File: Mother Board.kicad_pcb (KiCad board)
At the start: 4 copper layers, 93 x 151 mm, 103 parts, among them J1 Conn_01x04, J2 USB_B_Mini, J3 Conn_02x05_Odd_Even, J4 Conn_01x04, J5 Conn_01x03, J6 Conn_01x03, J7 Conn_01x04, SW1 SW_Push, U1 SC189, U2 TPS2121, U3 FT232RL, U4 TPS2121, U5 STM32F407VGTx, U6 W25Q128JV-DTR, U7 SN74LVC1G04DBVR, Y1 Crystal_GND24

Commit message: Needs final clean up, then ready for ordering
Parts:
- added 3v3_MUX_ST1: TestPoint, TestPoint:TestPoint_Pad_D1.0mm, F.Cu at (101.5, 143.5)
- added 5V_MUX_ST1: TestPoint, TestPoint:TestPoint_Pad_D1.0mm, F.Cu at (96.5, 143.5)
- added D10: LED, LED_SMD:LED_1206_3216Metric_Pad1.42x1.75mm_HandSolder, F.Cu at (104.5, 64.0)
- added D11: LED, LED_SMD:LED_1206_3216Metric_Pad1.42x1.75mm_HandSolder, F.Cu at (98.0, 64.0)
- added D5: LED, LED_SMD:LED_1206_3216Metric_Pad1.42x1.75mm_HandSolder, F.Cu at (172.0, 177.0)
- added D6: LED, LED_SMD:LED_1206_3216Metric_Pad1.42x1.75mm_HandSolder, F.Cu at (160.5, 64.0)
- added D7: LED, LED_SMD:LED_1206_3216Metric_Pad1.42x1.75mm_HandSolder, F.Cu at (154.0, 64.0)
- added D8: LED, LED_SMD:LED_1206_3216Metric_Pad1.42x1.75mm_HandSolder, F.Cu at (132.5, 64.0)
- added D9: LED, LED_SMD:LED_1206_3216Metric_Pad1.42x1.75mm_HandSolder, F.Cu at (126.0, 64.0)
- added Q1: Q_NMOS_GSD, Package_TO_SOT_SMD:SOT-323_SC-70_Handsoldering, F.Cu at (172.0, 185.0)
- added Q2: Q_NMOS_GSD, Package_TO_SOT_SMD:SOT-323_SC-70_Handsoldering, F.Cu at (160.5, 72.0)
- added Q3: Q_NMOS_GSD, Package_TO_SOT_SMD:SOT-323_SC-70_Handsoldering, F.Cu at (154.0, 72.0)
- added Q4: Q_NMOS_GSD, Package_TO_SOT_SMD:SOT-323_SC-70_Handsoldering, F.Cu at (132.5, 72.0)
- added Q5: Q_NMOS_GSD, Package_TO_SOT_SMD:SOT-323_SC-70_Handsoldering, F.Cu at (126.0, 72.0)
- added Q6: Q_NMOS_GSD, Package_TO_SOT_SMD:SOT-323_SC-70_Handsoldering, F.Cu at (104.5, 72.0)
- added Q7: Q_NMOS_GSD, Package_TO_SOT_SMD:SOT-323_SC-70_Handsoldering, F.Cu at (98.0, 72.0)
- added R10: 10k, Resistor_SMD:R_0603_1608Metric_Pad1.05x0.95mm_HandSolder, F.Cu at (172.0, 190.0)
- added R11: 330R, Resistor_SMD:R_0603_1608Metric_Pad1.05x0.95mm_HandSolder, F.Cu at (172.0, 180.5)
- added R44: 10k, Resistor_SMD:R_0603_1608Metric_Pad1.05x0.95mm_HandSolder, F.Cu at (160.5, 77.0)
- added R45: 10k, Resistor_SMD:R_0603_1608Metric_Pad1.05x0.95mm_HandSolder, F.Cu at (154.0, 77.0)
- added R46: 330R, Resistor_SMD:R_0603_1608Metric_Pad1.05x0.95mm_HandSolder, F.Cu at (160.5, 67.0)
- added R47: 330R, Resistor_SMD:R_0603_1608Metric_Pad1.05x0.95mm_HandSolder, F.Cu at (154.0, 67.0)
- added R48: 10k, Resistor_SMD:R_0603_1608Metric_Pad1.05x0.95mm_HandSolder, F.Cu at (132.5, 77.0)
- added R49: 10k, Resistor_SMD:R_0603_1608Metric_Pad1.05x0.95mm_HandSolder, F.Cu at (126.0, 77.0)
- added R50: 330R, Resistor_SMD:R_0603_1608Metric_Pad1.05x0.95mm_HandSolder, F.Cu at (132.5, 67.5)
- added R51: 330R, Resistor_SMD:R_0603_1608Metric_Pad1.05x0.95mm_HandSolder, F.Cu at (126.0, 67.5)
- added R52: 10k, Resistor_SMD:R_0603_1608Metric_Pad1.05x0.95mm_HandSolder, F.Cu at (104.6, 77.0)
- added R53: 10k, Resistor_SMD:R_0603_1608Metric_Pad1.05x0.95mm_HandSolder, F.Cu at (98.0, 77.0)
- added R54: 330R, Resistor_SMD:R_0603_1608Metric_Pad1.05x0.95mm_HandSolder, F.Cu at (104.6, 67.5)
- added R55: 330R, Resistor_SMD:R_0603_1608Metric_Pad1.05x0.95mm_HandSolder, F.Cu at (98.0, 67.5)
- added SPI_FLASH_CS1: TestPoint, test_points_mdg:TestPoint_Keystone_5015_Micro-Minature, F.Cu at (123.5, 121.0)
- added USART3_CTS1: TestPoint, test_points_mdg:TestPoint_Keystone_5015_Micro-Minature, F.Cu at (129.5, 201.0)
- added USART3_RTS1: TestPoint, test_points_mdg:TestPoint_Keystone_5015_Micro-Minature, F.Cu at (134.5, 201.0)
- added USART3_RX1: TestPoint, test_points_mdg:TestPoint_Keystone_5015_Micro-Minature, F.Cu at (124.5, 201.0)
- added USART3_TX1: TestPoint, test_points_mdg:TestPoint_Keystone_5015_Micro-Minature, F.Cu at (119.5, 201.0)
- GND1, GND2, GND3, GND4, GND5, I2C1_SCL1, I2C1_SDA1, SPI3_MISO1, SPI3_MOSI1, SPI3_SCK1: footprint test_points_mdg:Keystone_5010 -> test_points_mdg:TestPoint_Keystone_5015_Micro-Minature
- moved GND1 5.00 mm to (87.5, 63.0)
- moved REF** 5.00 mm to (143.0, 67.0)
- moved REF** 5.00 mm to (171.0, 67.0)
- moved REF** 5.00 mm to (115.0, 67.0)
- moved GND3 1.00 mm to (172.0, 76.0)
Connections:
- U5 pad 33: Net-(U5-Pad33) -> MICRO_STATUS
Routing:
- net CARD0_ENABLE: track 114.7 -> 187.0 mm, vias 1 -> 2
- net +3V3: track 110.8 -> 179.2 mm, vias 33 -> 40
- net CARD0_STATUS: track 128.4 -> 169.8 mm, vias 1 -> 2
- net MICRO_STATUS: track 0.00 -> 41.2 mm, vias 0 -> 2
- net GND: track 116.4 -> 157.5 mm, vias 69 -> 86
- net CARD4_ENABLE: track 229.4 -> 260.5 mm
- net CARD4_STATUS: track 239.1 -> 264.1 mm
- net CARD1_ENABLE: track 203.1 -> 224.5 mm, vias 1 -> 2
- net Net-(3v3_MUX_ST1-Pad1): track 4.05 -> 20.8 mm
- net CARD1_STATUS: track 211.2 -> 226.0 mm, vias 1 -> 2
- net Net-(5V_MUX_ST1-Pad1): track 17.2 -> 29.2 mm
- net USART3_CTS: track 63.7 -> 69.9 mm
- net USART3_RX: track 51.6 -> 57.1 mm
- net Net-(Q3-Pad3): track 0.00 -> 4.03 mm
- net Net-(Q2-Pad3): track 0.00 -> 4.03 mm
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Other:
- board size 93 x 151 mm -> 93 x 146 mm
- board text added: "24V 24V 5V 5V"
- board text added: "24V 24V 5V 5V 3.3V 3.3V GND GND I2C1_SDA I2C1_SCL ADD0 ADD1 ADD2 ENABLE STATUS GPIO5 GPIO4 GPIO3 GPIO2 SENSE+ GND GND"
- board text added: "24V 24V 5V 5V 3.3V 3.3V GND GND SPI3_SCK SPI3_MISO SPI3_MOSI CS TIM1CH1 TIM1CH1N TIM3CH1 TIM2CH1 TIM9CH1 GPIO0 GPIO1 SENSE- GND GND"
- board text added: "24V 24V 5V 5V 3.3V 3.3V GND GND SPI3_SCK SPI3_MISO SPI3_MOSI CS TIM8_CH1 TIM8_CH1N TIM5_CH1 TIM4_CH1 TIM12_CH2 GPIO0 GPIO1 SENSE - GND GND"
- board text added: "3V3 3V3 GND GND"
- board text added: "3V3 STAT"
- board text added: "5V STAT"
- board text added: "CARD0"
- board text added: "CARD0 ENABLE"
- board text added: "CARD0 STATUS"
- board text added: "CARD1"
- board text added: "CARD1 ENABLE"
- board text added: "CARD1 STATUS"
- board text added: "CARD4"
- board text added: "CARD4 ENABLE"
- board text added: "CARD4 STATUS"
- board text added: "GND GND GND GND"
- board text added: "MICRO STATUS"
- board text added: "RESET"
- board text added: "RX"
- board text added: "TX"

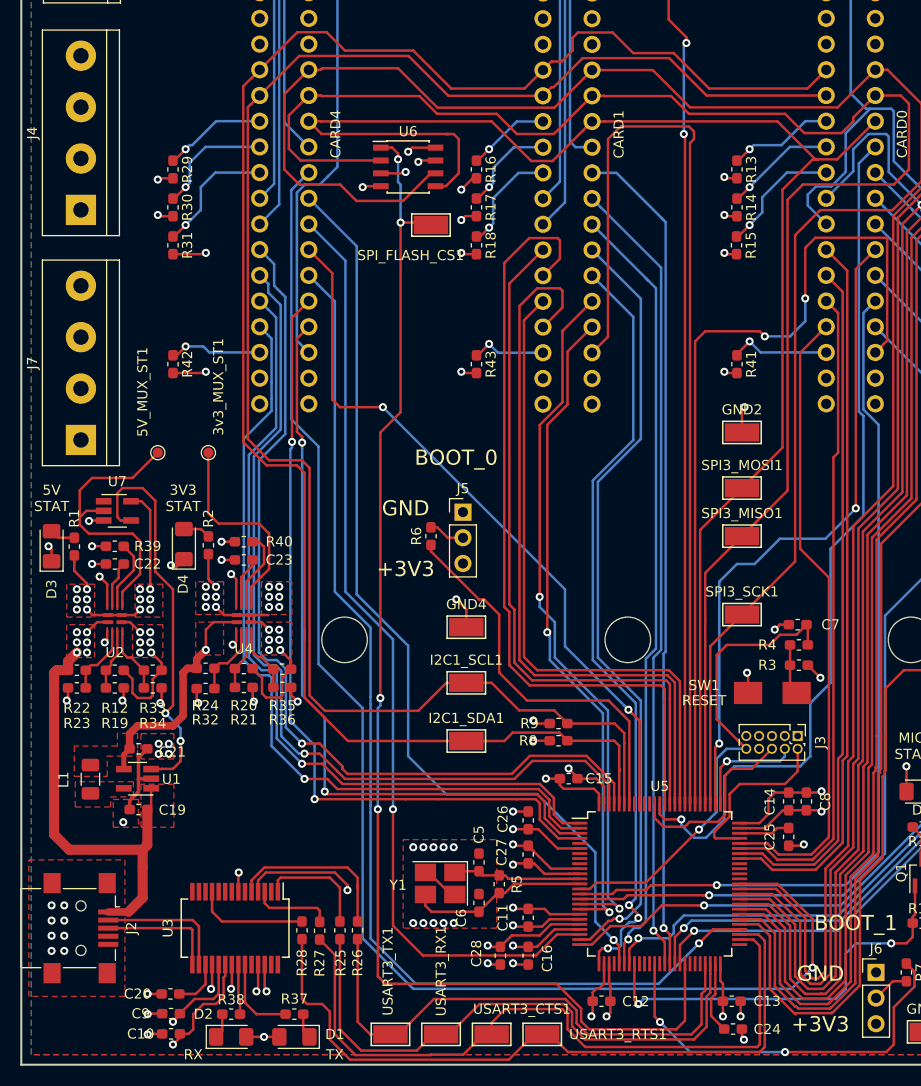
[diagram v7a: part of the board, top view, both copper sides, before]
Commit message: added part numbers to schematic, pcb ordered
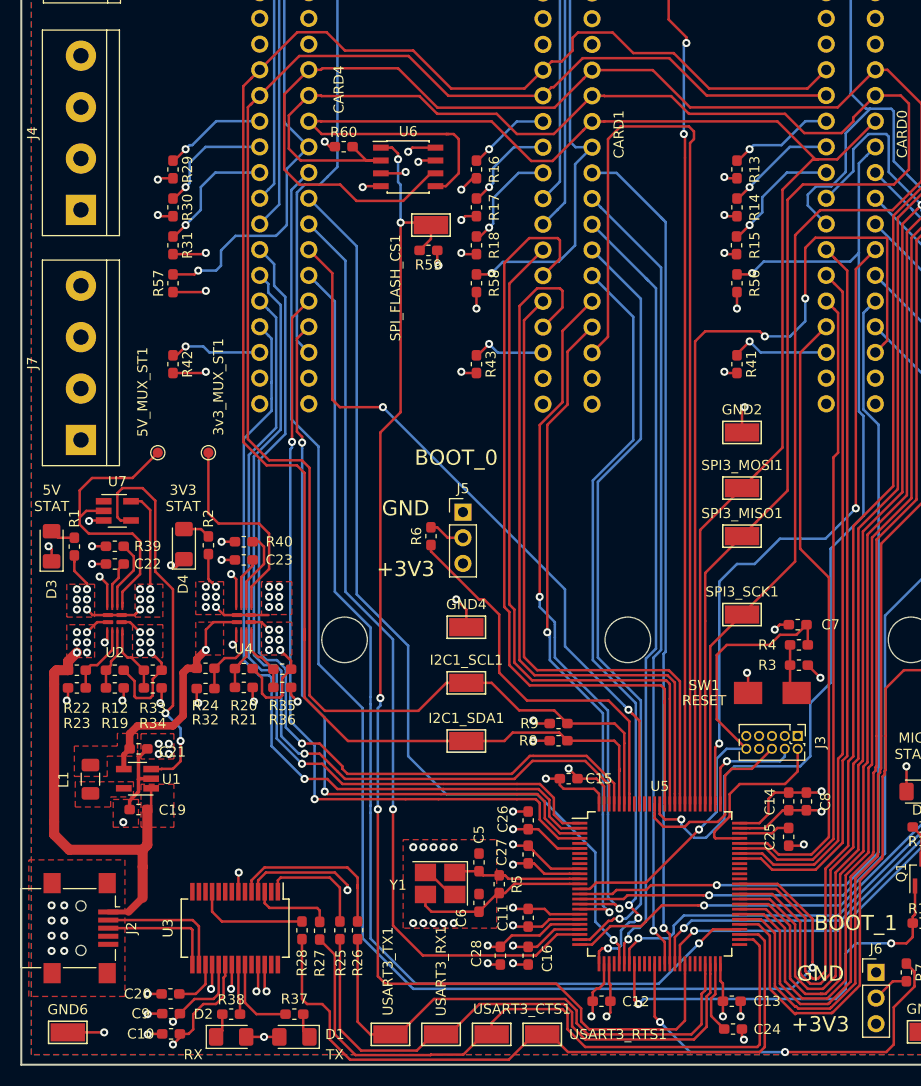
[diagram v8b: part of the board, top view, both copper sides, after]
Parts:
- added GND6: TestPoint, test_points_mdg:TestPoint_Keystone_5015_Micro-Minature, F.Cu at (87.6, 200.8)
- added R56: 10k, Resistor_SMD:R_0603_1608Metric_Pad1.05x0.95mm_HandSolder, F.Cu at (153.8, 126.8)
- added R57: 10k, Resistor_SMD:R_0603_1608Metric_Pad1.05x0.95mm_HandSolder, F.Cu at (98.0, 126.8)
- added R58: 10k, Resistor_SMD:R_0603_1608Metric_Pad1.05x0.95mm_HandSolder, F.Cu at (128.0, 126.8)
- added R59: 10k, Resistor_SMD:R_0603_1608Metric_Pad1.05x0.95mm_HandSolder, F.Cu at (123.2, 123.5)
- added R60: 10k, Resistor_SMD:R_0603_1608Metric_Pad1.05x0.95mm_HandSolder, F.Cu at (114.9, 113.2)
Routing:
- net CARD4_CS: track 236.4 -> 259.2 mm, vias 1 -> 2
- net CARD1_CS: track 211.2 -> 232.6 mm, vias 1 -> 2
- net CARD0_CS: track 86.3 -> 99.2 mm, vias 1 -> 2
- net +3V3: track 179.2 -> 188.5 mm, vias 40 -> 45
- net GND: track 157.5 -> 161.1 mm, vias 86 -> 87
- net SPI3_MISO: track 164.6 -> 168.0 mm
- net SPI_FLASH_CS: track 126.7 -> 129.6 mm
